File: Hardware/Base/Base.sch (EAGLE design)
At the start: 74 parts, among them IC1 74LS245N, T1 2N3904, T10 2N3904, T11 2N3904, T12 2N3904, T2 2N3904, T3 2N3904, T4 2N3904, T5 2N3904, T6 2N3904, T7 2N3904, T8 2N3904, T9 2N3904

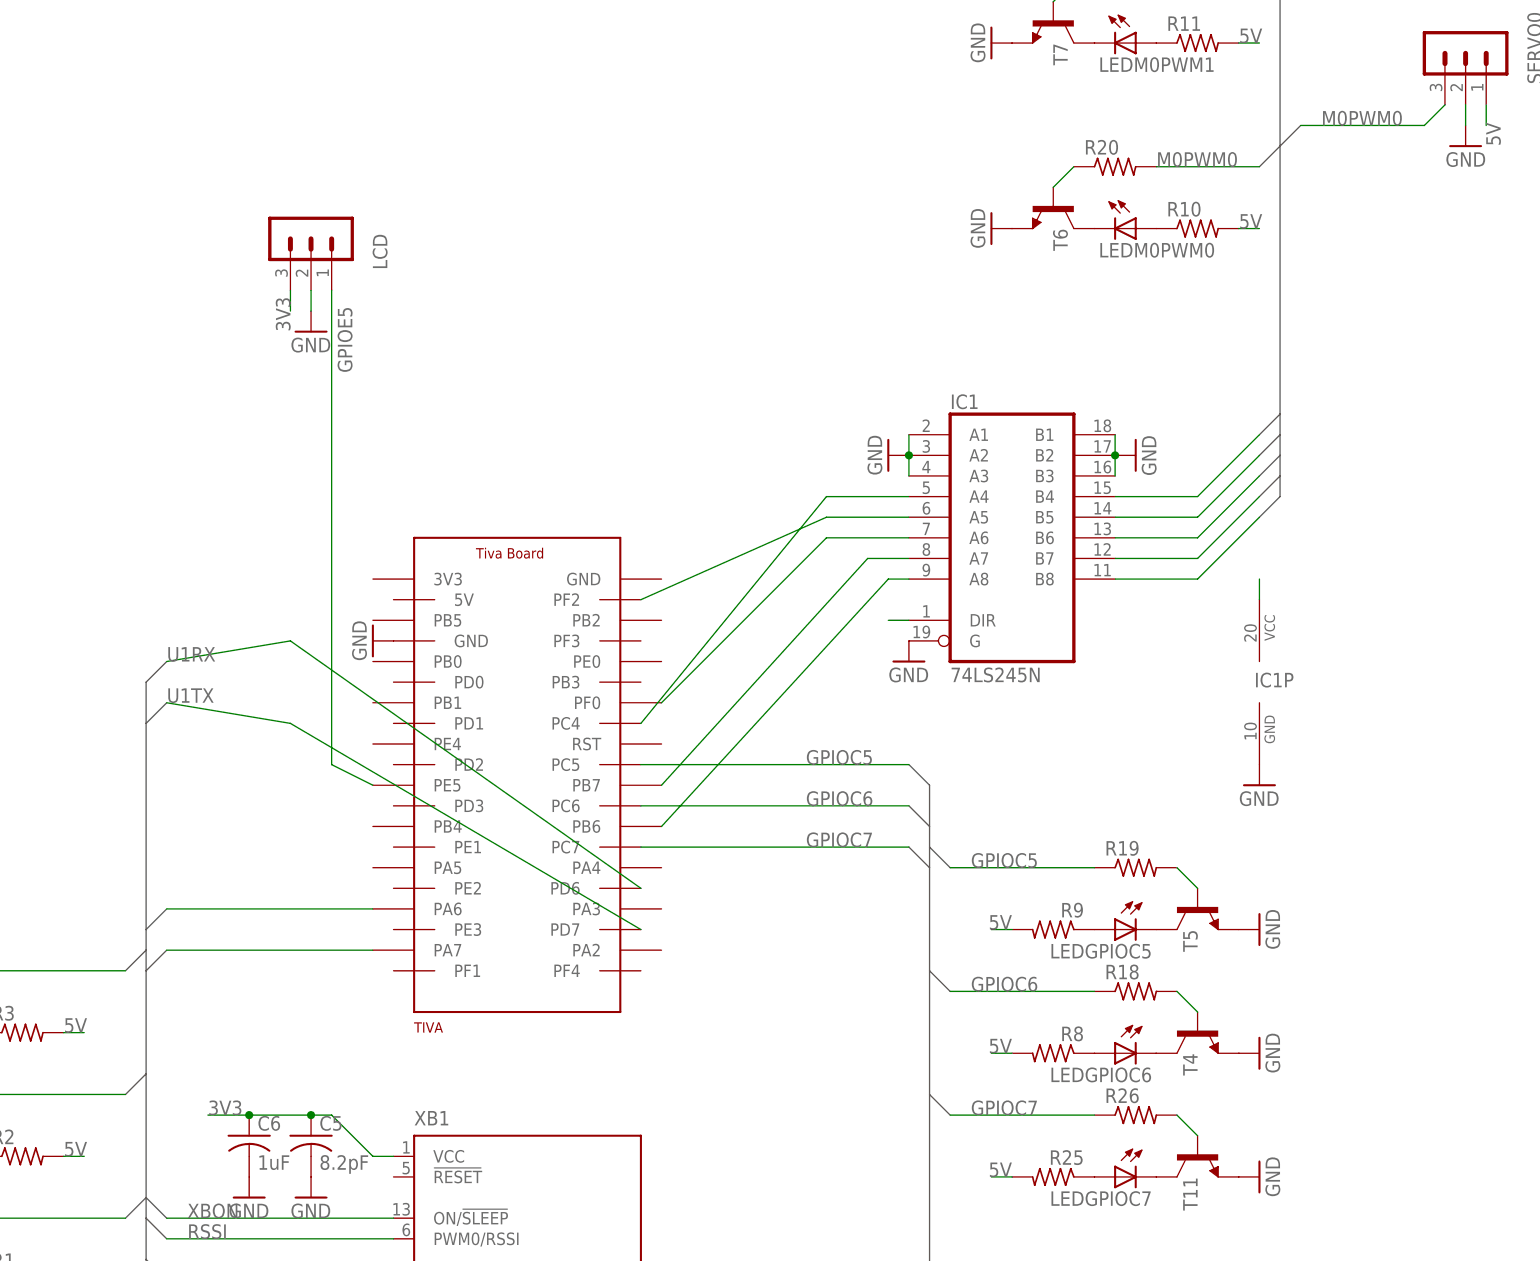
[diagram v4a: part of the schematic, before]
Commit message: Wires prettied up in Base.brd/sch
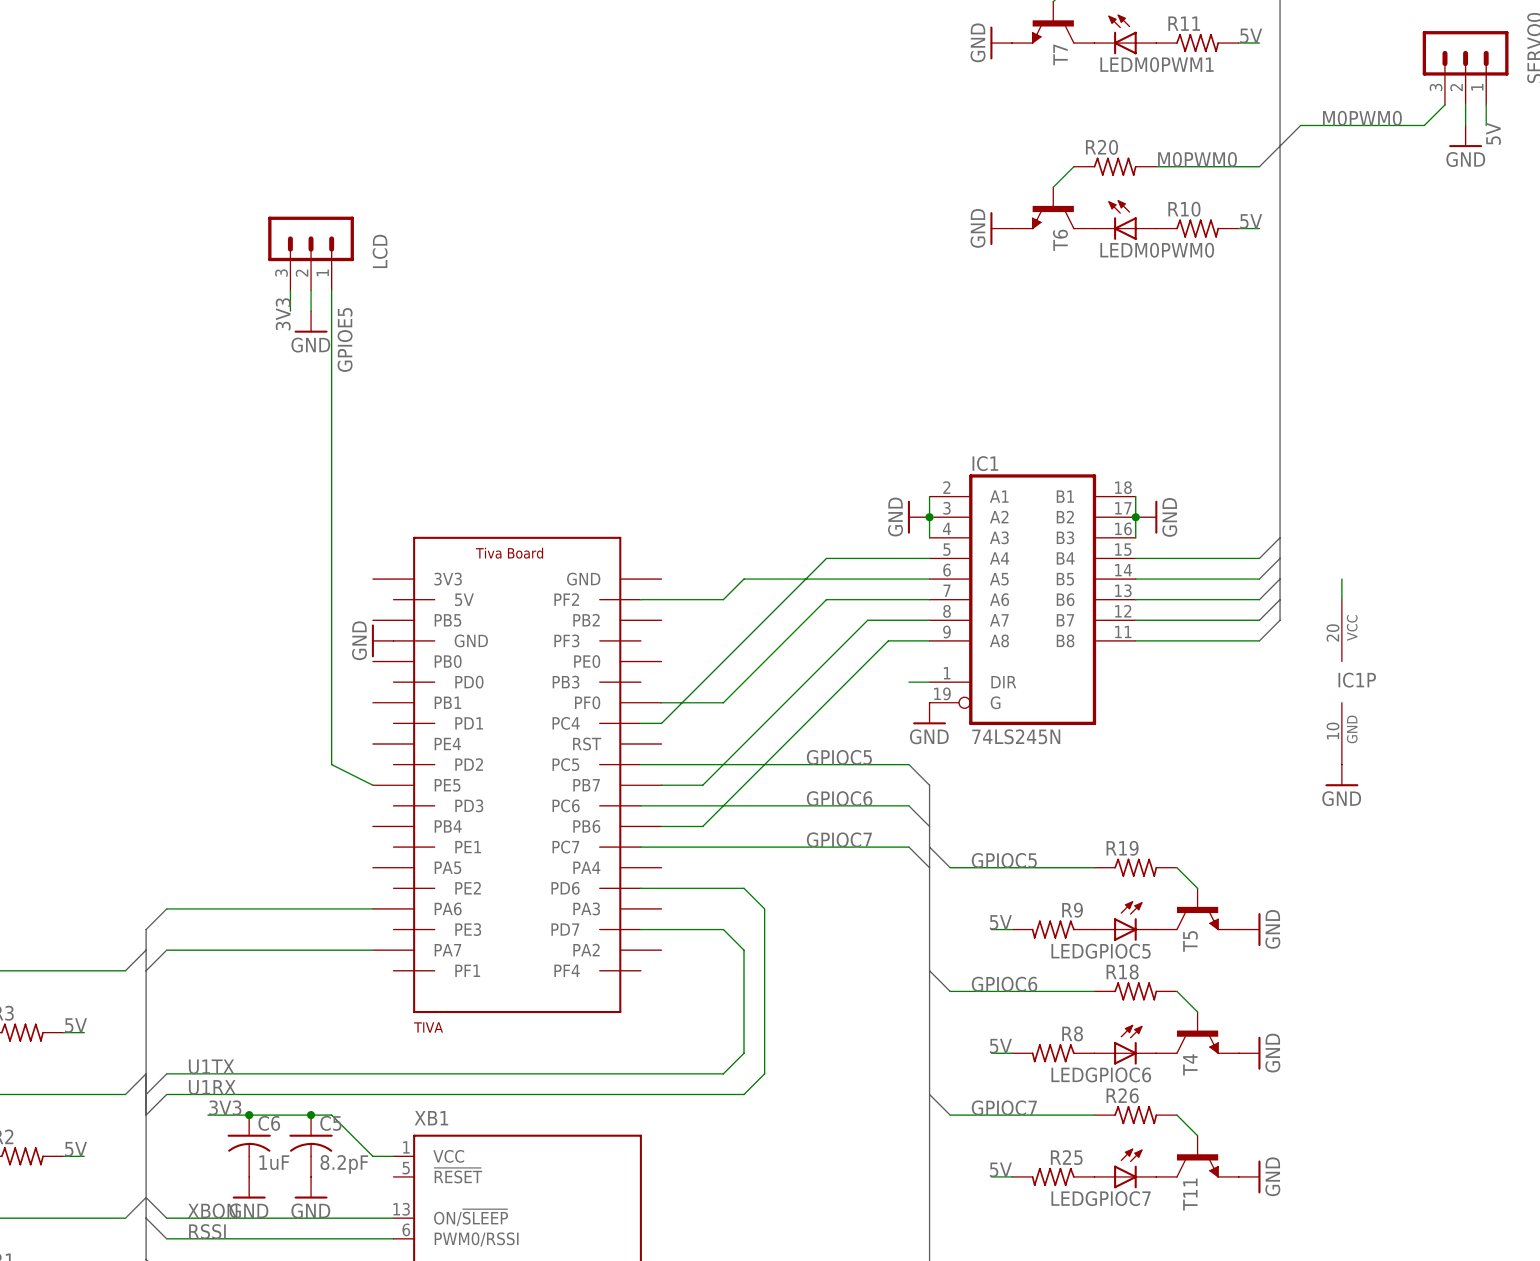
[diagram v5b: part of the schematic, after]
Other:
- moved on the sheet: IC1, IC1P
